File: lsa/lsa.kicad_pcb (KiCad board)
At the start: 2 copper layers, 61.9 x 24.2 mm, 43 parts, among them J2 Conn_01x08_Pin, U1 TCRT5000, U2 TCRT5000, U3 TCRT5000, U4 TCRT5000, U5 TCRT5000

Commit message: Switching to 10 pin FFC cable on both board and LSA, modifying silkscreen and holes for MPU
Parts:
- removed kibuzzard-6A8B4B44: G***, kibuzzard-6A8B4B44
- added kibuzzard-6A96670D: G***, kibuzzard-6A96670D, F.Cu at (116.3, 73.8)
- added kibuzzard-6A966794: G***, kibuzzard-6A966794, B.Cu at (116.5, 75.2)
- J2: value Conn_01x08_Pin -> Conn_01x10_Pin; footprint Connector_FFC-FPC:JUSHUO_AFA07-S08FCA-00_1x8-1MP_P1.0mm_Horizontal -> Connector_FFC-FPC:JUSHUO_AFA07-S10FCA-00_1x10-1MP_P1.0mm_Horizontal
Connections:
- J2 pad 1: +3V3 -> /A4_32
- J2 pad 2: +3V3 -> /A3_35
- J2 pad 3: GND -> /A2_34
- J2 pad 4: /A0_36 -> /A1_39
- J2 pad 5: /A1_39 -> /A0_36
- J2 pad 6: /A2_34 -> GND
- J2 pad 7: /A3_35 -> +3V3
- J2 pad 8: /A4_32 -> +3V3
- J2 pad MP: (no net) -> GND
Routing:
- net /A4_32: track 38.3 -> 26.3 mm
- net /A0_36: track 41.9 -> 30.8 mm, vias 1 -> 0
- net /A3_35: track 27.5 -> 18.2 mm, vias 1 -> 0
- net /A1_39: track 21.2 -> 26.1 mm, vias 1 -> 0
- net +3V3: track 120.2 -> 118.0 mm
- net /A2_34: track 17.6 -> 19.3 mm
- net GND: vias 0 -> 1
- added copper zone on F.Cu, net GND

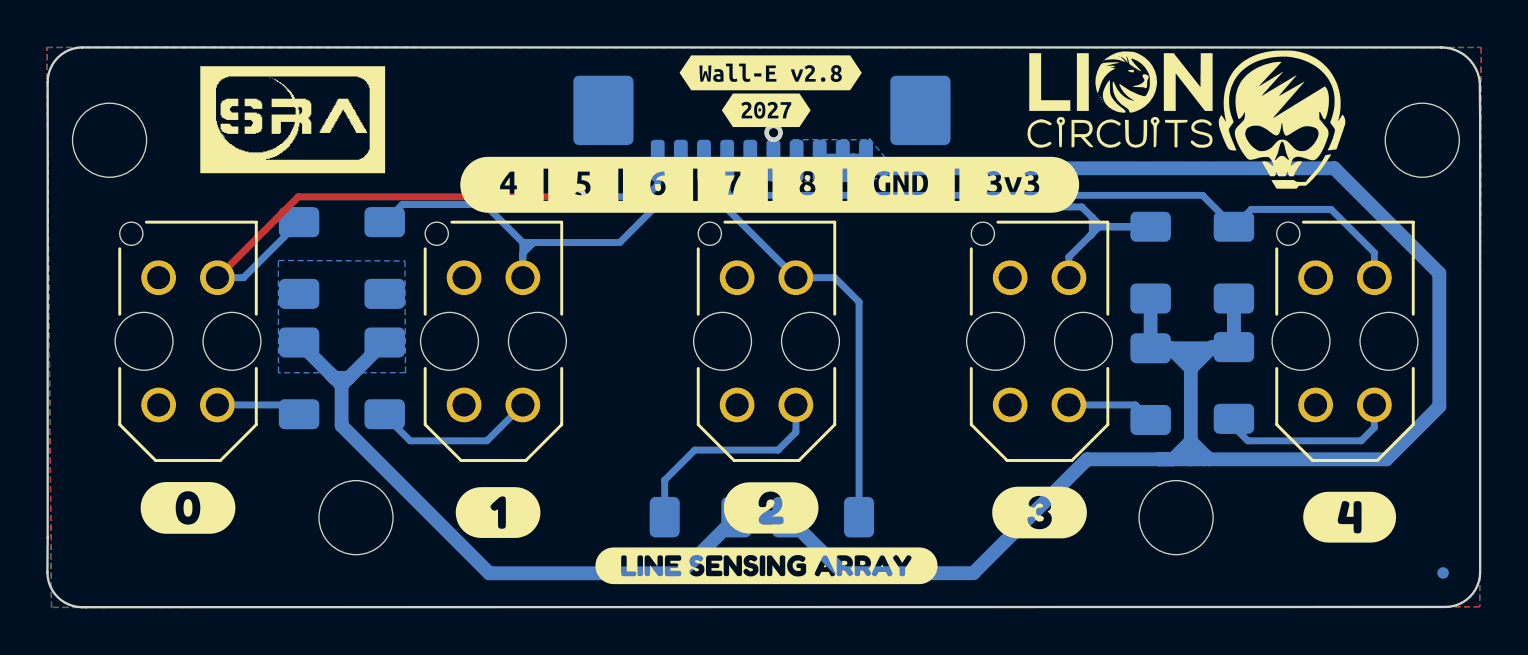
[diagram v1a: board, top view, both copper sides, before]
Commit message: Changing the footprint for boot/reset buttons and adding step file for USB-C
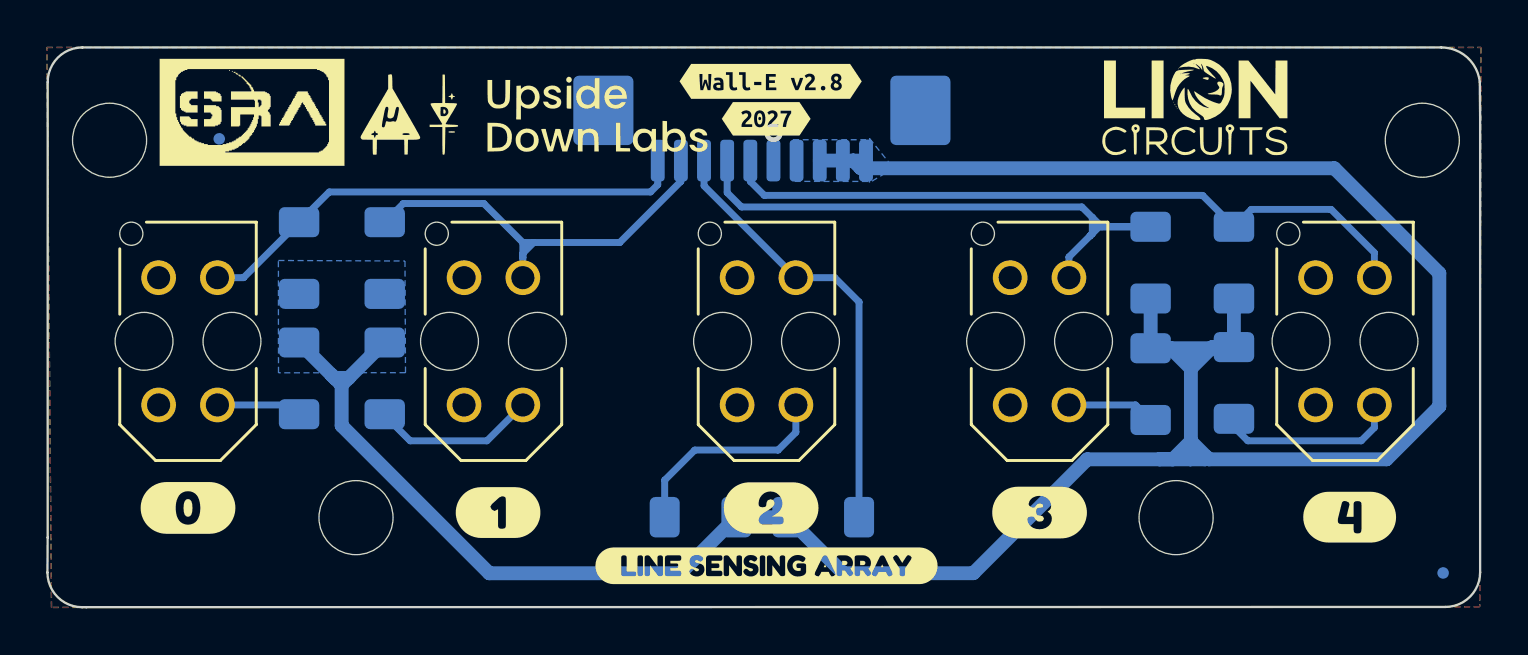
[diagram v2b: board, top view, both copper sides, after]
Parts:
- removed the G*** at (101.2, 70.6)
- removed the kibuzzard-672CF9E4 at (133.8, 71.0)
- removed the kibuzzard-6A70DDC1 at (116.4, 69.0)
- removed the kibuzzard-6A70DDE3 at (116.2, 70.6)
- removed kibuzzard-6A96670D: G***, kibuzzard-6A96670D
- removed kibuzzard-6A966794: G***, kibuzzard-6A966794
- added G***: LOGO, LOGO, F.Cu at (106.2, 70.8)
- added kibuzzard-6AC3C74E: G***, kibuzzard-6AC3C74E, B.Cu at (116.4, 74.5)
- G***: moved to B.Cu
- moved G*** 8.30 mm to (130.2, 71.2), turned to 180 degrees
- moved G*** 3.25 mm to (134.7, 70.5)
- moved G*** 1.79 mm to (94.0, 70.7)
- moved kibuzzard-6A70DDC1 0.37 mm to (116.4, 69.4)
- moved kibuzzard-6A70DDE3 0.37 mm to (116.2, 71.0)
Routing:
- net /A4_32: track 26.3 -> 21.7 mm, vias 1 -> 0
